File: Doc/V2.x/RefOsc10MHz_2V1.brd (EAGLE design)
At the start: 90 x 70 mm, 77 parts, among them CON1 TYCO-AMP_USBUSB-B_SMT, CON11 MCX-J-P-X-RA-SM1, CON2 HEADER-2X5SMD, CON3 SD-73100-0105, CON4 AVR-ISP-6SMD, CON5 AVR-JTAG-10SMD, CON6 HEADER-2X3SMD, IC1 ATmega328-P, IC11 712-RXM-GNSS-TM-B, IC2 LC4032V_XXT44, IC3 74HCT221D, IC4 CFPT-141, IC5 LMH6645MF, IC6 LM2831YMF

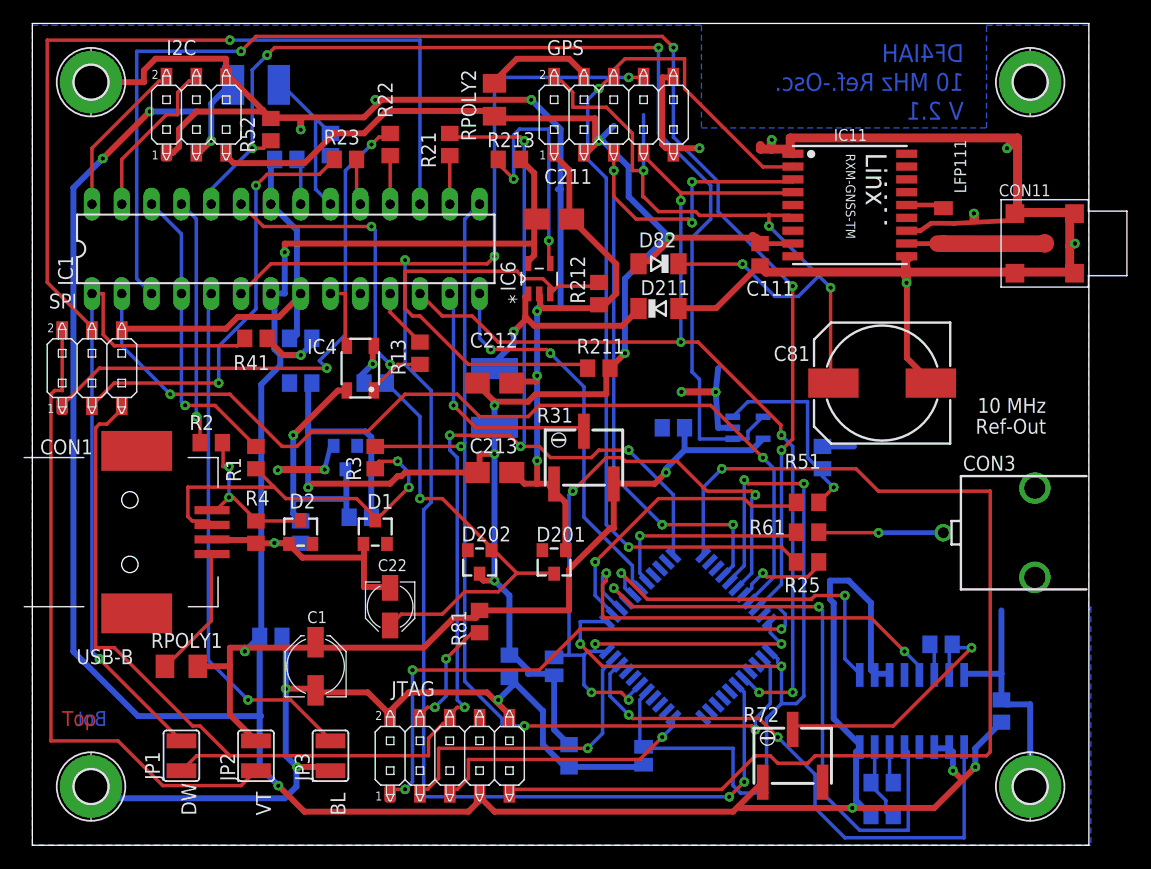
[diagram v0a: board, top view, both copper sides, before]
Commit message: avr_DF4IAH_Bootloader - Doc - Eagle: V2.1 - OP-Amps U4 and U5 added/changed
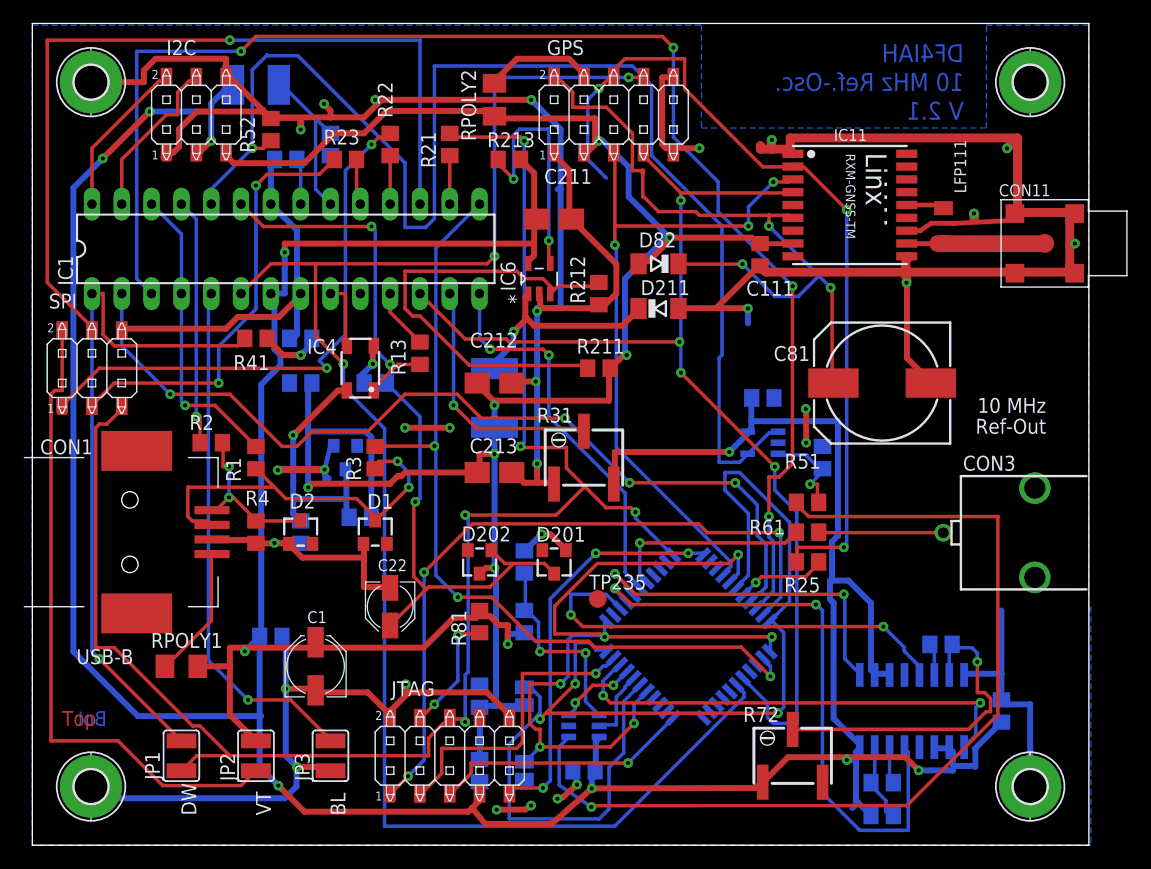
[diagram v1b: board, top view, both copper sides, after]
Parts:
- removed IC5: LMH6645MF, df4iah:SOT95P280X145-5N
- added C941: 100n, rcl:C0805
- added R941: 10k, rcl:R0805
- added R942: 22k, rcl:R0805
- added TP235: TPTP15R, testpad:TP15R
- added U4: OPA357, df4iah_opamp:SOT-23-6
- added U5: OPA354, df4iah_opamp:SOT-23-5
- C71: value 10p -> 0p
- C911, C921, C922, C931, C951: value 10n -> 100n
- R221: value 56 -> 68
- moved SJ21 10.2 mm to (41.9, 6.35)
- moved C951 8.03 mm to (62.2, 38.1), turned to 180 degrees
- moved C921 7.73 mm to (38.1, 6.35)
- moved SJ22 3.59 mm to (41.9, 12.7)
- moved C922 3.59 mm to (38.1, 12.7), turned to 90 degrees
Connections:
- net GATE renamed GATE_IN
- net GATE_TRIG renamed GATE_TRIG_OUT
- net SYNC renamed SYNC_IN
- new net N$6: R941.2, R942.1, U4.4
- new net OP_ENA: IC2.29, U4.5
- new net OP_IN: IC2.30, U4.3
- new net PHASE_OUT: IC2.35, TP235.TP
- net ADC_PHASE: now also U5.1, U5.4; no longer IC5.1, IC5.4
- net ADC_PHASE_PULLHOLD: now also U5.3; no longer IC5.3
- net GND: now also C941.2, R941.1, U4.2, U5.2; no longer IC5.2
- net PHASE_ERROR: now also U4.1; no longer IC2.35
- net VCC: now also C941.1, R942.2, U4.6, U5.5; no longer IC5.5
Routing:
- net JTAG_TDI: track 96.9 -> 34.8 mm, vias 1 -> 3
- net PHASE_ERROR: track 24.9 -> 80.3 mm
- net VCC_3V3_SJ2: track 73.1 -> 100.9 mm, vias 6 -> 3
- net ADC_PHASE: track 92.8 -> 113.4 mm, vias 3 -> 1
- net N$6: track 0.00 -> 17.1 mm, vias 0 -> 2
- net GND_SJ1: track 89.0 -> 73.5 mm, vias 4 -> 6
- net VCC: track 350.9 -> 363.6 mm, vias 11 -> 12
- net GND: track 420.8 -> 408.3 mm, vias 21 -> 30
- net JTAG_TCK: track 48.7 -> 60.0 mm
- net N_USB_DISC: track 82.7 -> 72.2 mm
- net ADC_PHASE_PULLHOLD: track 17.3 -> 8.51 mm
- net GPS_NMEA_RX: track 66.2 -> 58.2 mm, vias 5 -> 3
- net GATE_TRIG_OUT: track 47.6 -> 40.0 mm
- net GPS_NMEA_TX: track 79.3 -> 72.4 mm, vias 2 -> 3
- net OP_IN: track 0.00 -> 6.79 mm, vias 0 -> 2
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
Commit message: avr_DF4IAH_Bootloader - Doc - Eagle: V2.1 - Sample&Hold - reduce from 10nF to 100pF, components are renamed
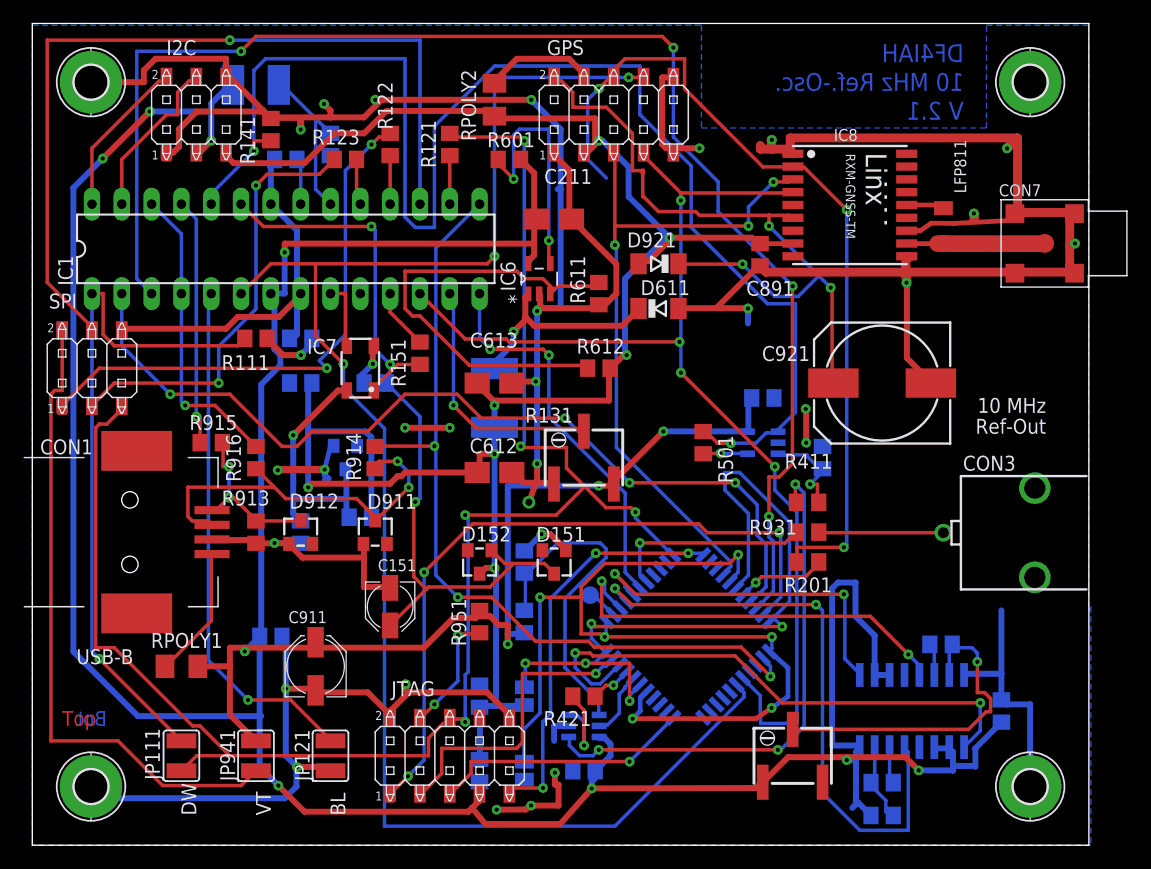
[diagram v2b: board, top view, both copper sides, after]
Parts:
- removed C1: 47uF, rcl:PANASONIC_C
- removed C81: 0.22F, rcl:140CLH-1010
- added C191, C291: 100n, rcl:C0805
- added R421, R501: 27, rcl:R0805
- C591: value 100n -> 10n
- C911: value 100n -> 47uF; device rcl:C0805 -> rcl:PANASONIC_C
- C921: value 100n -> 0.22F; device rcl:C0805 -> rcl:140CLH-1010
- moved C921 47.6 mm to (72.4, 39.4), flipped to the top, turned to 180 degrees
- moved C911 28.0 mm to (24.1, 15.2), flipped to the top, turned to 90 degrees
- moved TP235 0.73 mm to (47.5, 21.3), flipped to the bottom
- renumbered C111 to C891, C2 to C912, C203 to C611, C21 to C152, C212 to C613, C213 to C612, C22 to C151, C221 to C791, C31 to C101, C32 to C102, C51 to C411, C71 to C301, C72 to C311, C922 to C292, C931 to C391, C941 to C491, C951 to C591, CON11 to CON7, D1 to D911, D2 to D912, D201 to D151, D202 to D152, D211 to D611, D221 to D701, D82 to D921, H1 to H904, H2 to H901, H3 to H902, H4 to H903, IC11 to IC8, IC4 to IC7, JP1 to JP111, JP2 to JP941, JP3 to JP121, L211 to L611, L31 to L101, LFP111 to LFP811, R1 to R916, R13 to R151, R2 to R915, R21 to R121, R211 to R612, R212 to R611, R213 to R601, R22 to R122, R221 to R701, R23 to R123, R25 to R201, R3 to R914, R31 to R131, R4 to R913, R41 to R111, R51 to R411, R52 to R141, R61 to R931, R71 to R301, R72 to R311, R81 to R951, R941 to R401, R942 to R402, SJ21 to SJ201, SJ22 to SJ202
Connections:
- net ADC_PHASE_PULLHOLD renamed ADC_PHASE_SAMPLEHOLD
- new net OP_IN_R: R421.2, U4.3
- new net U5_FB: R501.2, U5.4
- net +3V3: now also C291.1; no longer C921.1
- net ADC_PHASE: now also R501.1; no longer U5.4
- net GND: now also C191.2, C291.2, C911.-, C921.-; no longer C1.-, C81.-, C911.2, C921.2
- net GPS_VBACKUP: now also C921.+; no longer C81.+
- net OP_IN: now also R421.1; no longer U4.3
- net VCC: now also C191.1, C911.+; no longer C1.+, C911.1
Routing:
- net PHASE_ERROR: track 80.3 -> 44.7 mm, vias 1 -> 3
- net VCC_3V3_SJ2: track 100.9 -> 66.6 mm, vias 3 -> 5
- net N$6: track 17.1 -> 28.3 mm, vias 2 -> 0
- net OP_IN_R: track 0.00 -> 8.17 mm, vias 0 -> 1
- net GATE_TRIG_OUT: track 40.0 -> 46.9 mm
- net GND: track 408.3 -> 414.8 mm
- net GND_SJ1: track 73.5 -> 79.5 mm
- net ADC_PHASE: track 113.4 -> 119.0 mm, vias 1 -> 2
- net U5_FB: track 0.00 -> 3.80 mm, vias 0 -> 1
- net GATE_IN: track 38.9 -> 35.6 mm
- net OP_IN: track 6.79 -> 3.60 mm, vias 2 -> 1
- net PHASE_OUT: track 0.00 -> 2.69 mm
- net VCC: track 363.6 -> 364.8 mm, vias 12 -> 13
- net GPS_PPS: track 95.1 -> 95.7 mm

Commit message: avr_DF4IAH_Bootloader - Doc - Eagle: V2.1 - Sample&Hold - reduce from 10nF to 100pF, components are renamed (2)
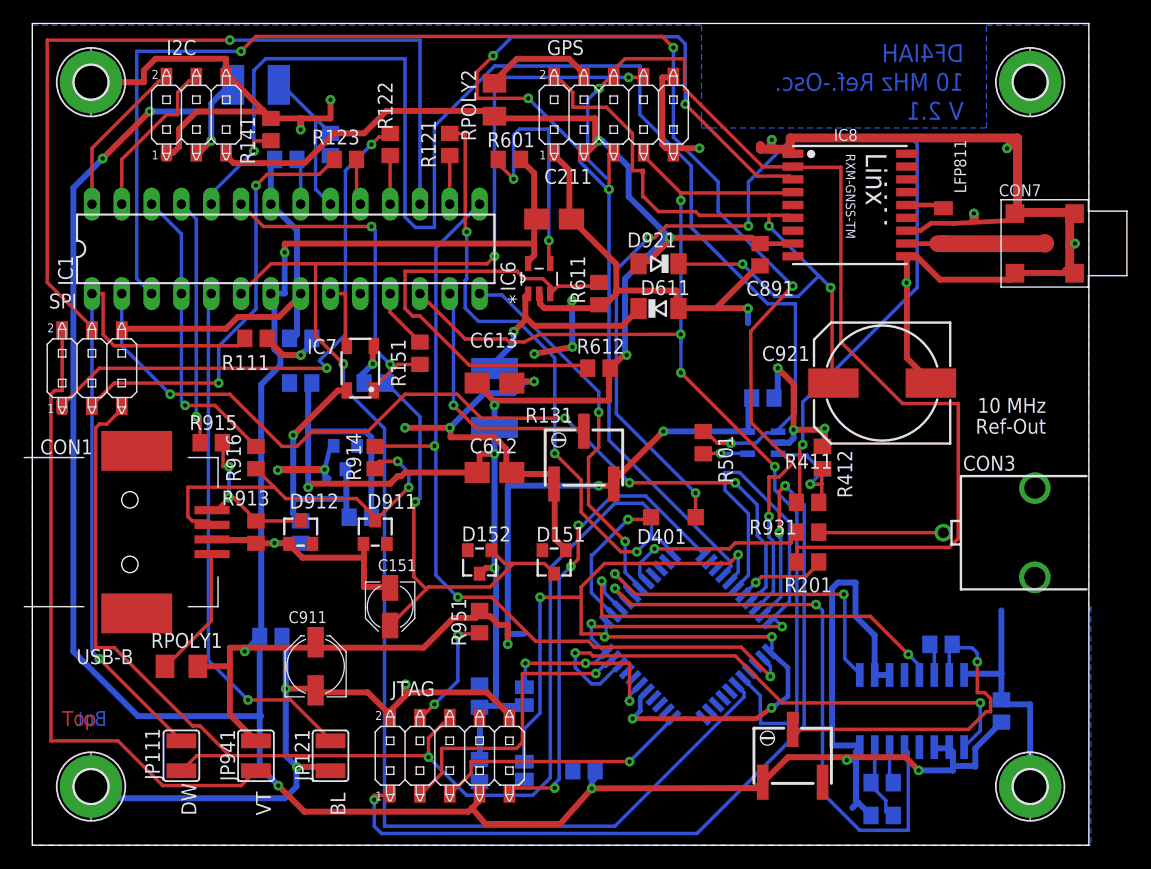
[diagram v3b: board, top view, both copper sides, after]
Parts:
- removed R401: 10k, rcl:R0805
- removed R402: 22k, rcl:R0805
- removed R421: 27, rcl:R0805
- removed TP235: TPTP15R, testpad:TP15R
- removed U4: OPA357, df4iah_opamp:SOT-23-6
- added D401: 1N4448, diode:SOD123
- added R412: 2M, rcl:R0805
- C411: value 10n -> 100p
- D151, D152: value BZX84-C2V7 -> BZX84-C3V6
- R411: value 1k -> 0R
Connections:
- removed net N$6: R401.2, R402.1, U4.4
- removed net OP_ENA: IC2.29, U4.5
- removed net OP_IN: IC2.30, R421.1
- removed net OP_IN_R: R421.2, U4.3
- removed net PHASE_OUT: IC2.35, TP235.TP
- new net PHASE_RSFF: D401.A, IC2.35
- net ADC_PHASE_SAMPLEHOLD: now also R412.2
- net GND: now also R412.1; no longer R401.1, U4.2
- net PHASE_ERROR: now also D401.C; no longer U4.1
- net VCC: no longer R402.2, U4.6
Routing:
- net PHASE_ERROR: track 44.7 -> 91.4 mm, vias 3 -> 4
- net GPS_NMEA_RX: track 58.2 -> 94.5 mm, vias 3 -> 4
- net GND: track 414.8 -> 379.1 mm, vias 30 -> 25
- net N$6: track 28.3 -> 0.00 mm
- net GPS_NMEA_TX: track 72.4 -> 90.2 mm, vias 3 -> 1
- net JTAG_TCK: track 60.0 -> 77.8 mm
- net PHASE_RSFF: track 0.00 -> 12.3 mm, vias 0 -> 1
- net JTAG_SRST: track 144.4 -> 156.7 mm, vias 5 -> 4
- net OP_IN_R: track 8.17 -> 0.00 mm, vias 1 -> 0
- net JTAG_TDI: track 34.8 -> 41.8 mm
- net OP_ENA: track 5.66 -> 0.00 mm
- net VCC: track 364.8 -> 360.7 mm
- net OP_IN: track 3.60 -> 0.00 mm, vias 1 -> 0
- net MCU_TXD: track 121.9 -> 124.7 mm
- net PHASE_OUT: track 2.69 -> 0.00 mm
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
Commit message: avr_DF4IAH_Bootloader - Doc - Eagle: V2.1 - PWM-Pull - drive not direct from AVR with unstabilized 5.0V but by the CPLD with its stabilized 3.3V instead.
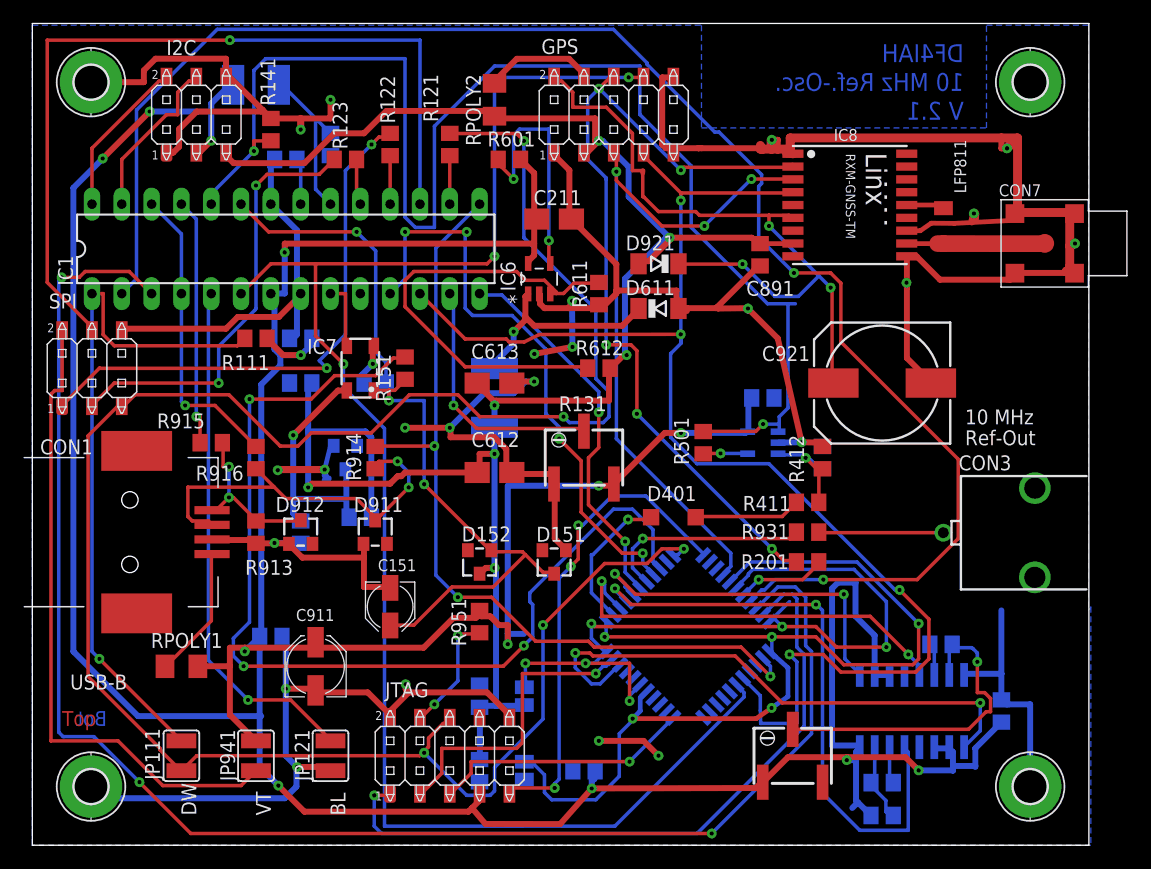
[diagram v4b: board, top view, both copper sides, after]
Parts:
- moved R151 1.80 mm to (31.8, 40.6)
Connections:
- removed net N_PWM_PULL: IC1.11, R151.1
- new net N_PWM_PULL_3V3: IC2.42, R151.1
- new net N_PWM_PULL_5V0: IC1.11, IC2.41
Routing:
- net N_PWM_PULL_3V3: track 0.00 -> 85.7 mm, vias 0 -> 3
- net PHASE_ERROR: track 91.4 -> 9.09 mm, vias 4 -> 0
- net MCU_RXD: track 77.2 -> 137.4 mm, vias 4 -> 2
- net N_PWM_PULL_5V0: track 0.00 -> 50.0 mm, vias 0 -> 4
- net GPS_NMEA_RX: track 94.5 -> 59.5 mm, vias 4 -> 3
- net JTAG_SRST: track 156.7 -> 180.2 mm, vias 4 -> 5
- net GPS_PPS: track 96.5 -> 119.3 mm
- net GPS_NMEA_TX: track 90.2 -> 71.5 mm, vias 1 -> 5
- net JTAG_TCK: track 77.8 -> 59.6 mm, vias 3 -> 1
- net GND: track 379.1 -> 392.8 mm, vias 25 -> 24
- net MCU_TXD: track 124.7 -> 135.9 mm, vias 4 -> 3
- net GND_SJ1: track 79.5 -> 90.4 mm, vias 6 -> 5
- net N_PWM_PULL: track 5.18 -> 0.00 mm
- net VCC_3V3_SJ2: track 66.6 -> 69.7 mm, vias 5 -> 6
- net C_10MHZ: track 16.5 -> 17.9 mm
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
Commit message: avr_DF4IAH_Bootloader - Doc - Eagle: V2.1 - R411 modified, CPLD pinout changed
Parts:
- R411: value 0R -> 2.7k
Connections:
- net N_PWM_PULL_3V3: now also IC2.43; no longer IC2.42
- net N_PWM_PULL_5V0: now also IC2.42; no longer IC2.41
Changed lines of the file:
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@@
 <attribute name="VALUE" x="67.6533625" y="26.040171875" size="1.27" layer="27"/>
 </element>
-<element name="R411" library="rcl" package="R0805" value="0R" x="66.04" y="29.21" smashed="yes">
+<element name="R411" library="rcl" package="R0805" value="2.7k" x="66.04" y="29.21" smashed="yes">
 <attribute name="NAME" x="60.5206625" y="28.482671875" size="1.27" layer="25"/>
 <attribute name="VALUE" x="67.651696875" y="28.567915625" size="1.27" layer="27"/>
@@
 <signal name="N_PWM_PULL_5V0">
 <contactref element="IC1" pad="11"/>
-<contactref element="IC2" pad="41"/>
 <wire x1="52" y1="24" x2="52.875" y2="23.125" width="0.3" layer="16"/>
 <wire x1="52" y1="24.875" x2="52" y2="24" width="0.3" layer="16"/>
@@
 <wire x1="31.75" y1="48.25" x2="31.75" y2="52.25" width="0.3" layer="16"/>
 <wire x1="30.5" y1="47" x2="31.75" y2="48.25" width="0.3" layer="16"/>
-<wire x1="52.875" y1="23.125" x2="52.910153125" y2="23.0125875" width="0.3" layer="16"/>
 <wire x1="30.5" y1="47" x2="30.48" y2="46.99" width="0.3" layer="16"/>
 <via x="52" y="24.875" extent="1-16" drill="0.35"/>
@@
 <via x="37" y="52.25" extent="1-16" drill="0.35"/>
 <via x="31.75" y="52.25" extent="1-16" drill="0.35"/>
+<contactref element="IC2" pad="42"/>
+<wire x1="52.875" y1="23.125" x2="53.4758375" y2="23.578275" width="0" layer="19" extent="16-16"/>
 </signal>
 <signal name="AREF">
@@
 <signal name="N_PWM_PULL_3V3">
 <contactref element="R151" pad="1"/>
-<contactref element="IC2" pad="42"/>
 <wire x1="30.75" y1="41.5" x2="31.75" y2="41.5" width="0.3" layer="1"/>
 <wire x1="29.25" y1="40" x2="30.75" y2="41.5" width="0.3" layer="1"/>
@@
 <wire x1="53.375" y1="23.625" x2="52.875" y2="24.125" width="0.3" layer="16"/>
 <wire x1="31.75" y1="41.5" x2="31.75" y2="41.59" width="0.3" layer="1"/>
-<wire x1="53.375" y1="23.625" x2="53.4758375" y2="23.578275" width="0.3" layer="16"/>
 <via x="18.5" y="38" extent="1-16" drill="0.35"/>
 <via x="18" y="15.25" extent="1-16" drill="0.35"/>
 <via x="41.875" y="17" extent="1-16" drill="0.35"/>
+<contactref element="IC2" pad="43"/>
+<wire x1="53.375" y1="23.625" x2="54.041525" y2="24.143959375" width="0" layer="19" extent="16-16"/>
 </signal>
 </signals>
